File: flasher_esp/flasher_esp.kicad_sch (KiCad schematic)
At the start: 20 parts, among them IC1 CP2102N-A02-GQFN24, J1 TYPE-C-31-M-12, J2 UART_NPWR, J3 UART_FLASH_ESP

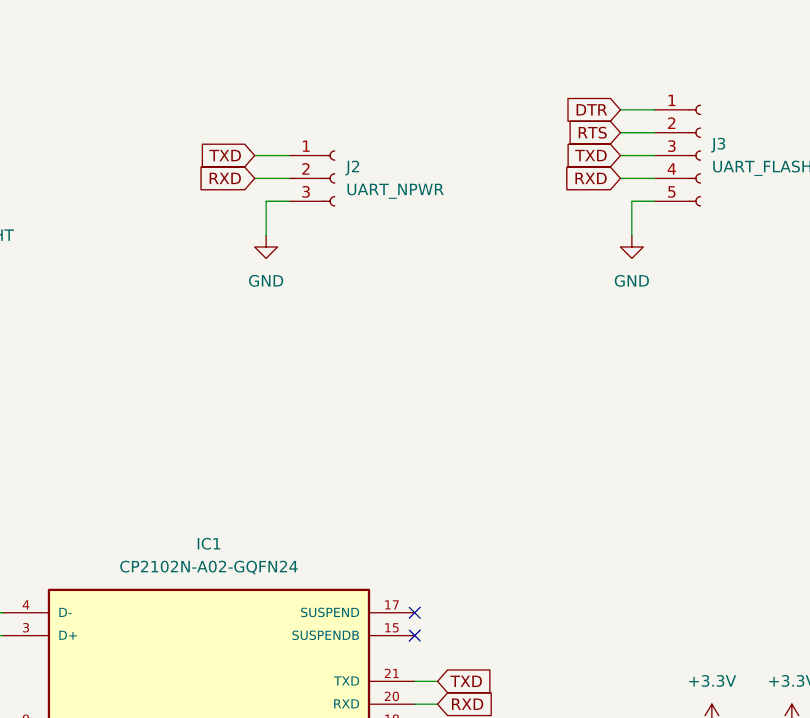
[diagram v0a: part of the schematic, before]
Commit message: [New] Complete PCB of flasher_esp
Signed-off-by: Homalozoa X <nx.tardis@gmail.com>
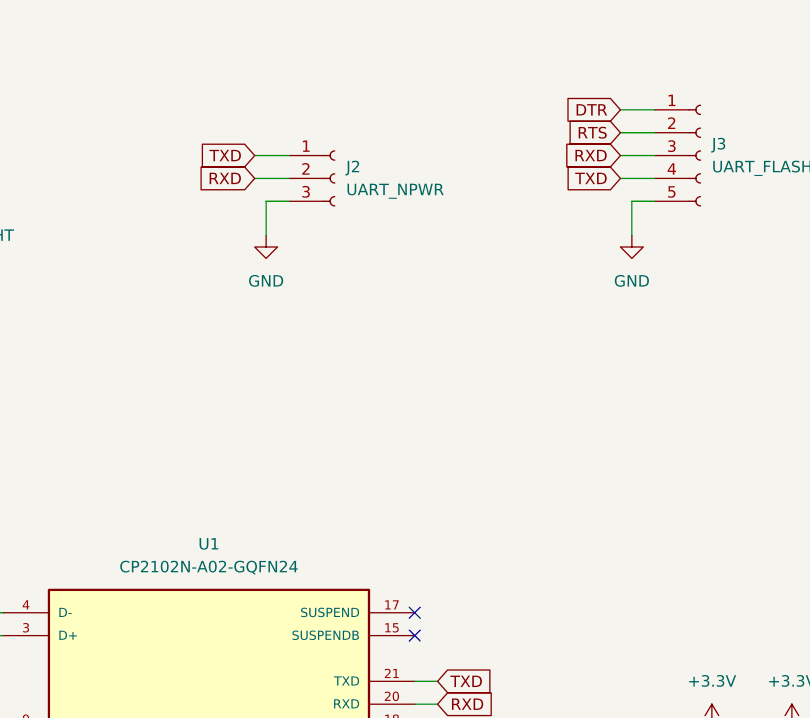
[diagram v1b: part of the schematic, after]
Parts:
- renumbered IC1 to U1
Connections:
- net RXD: now also J3.3 (Pin_3); no longer J3.4 (Pin_4)
- net TXD: now also J3.4 (Pin_4); no longer J3.3 (Pin_3)
